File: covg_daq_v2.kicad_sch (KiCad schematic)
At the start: 29 parts

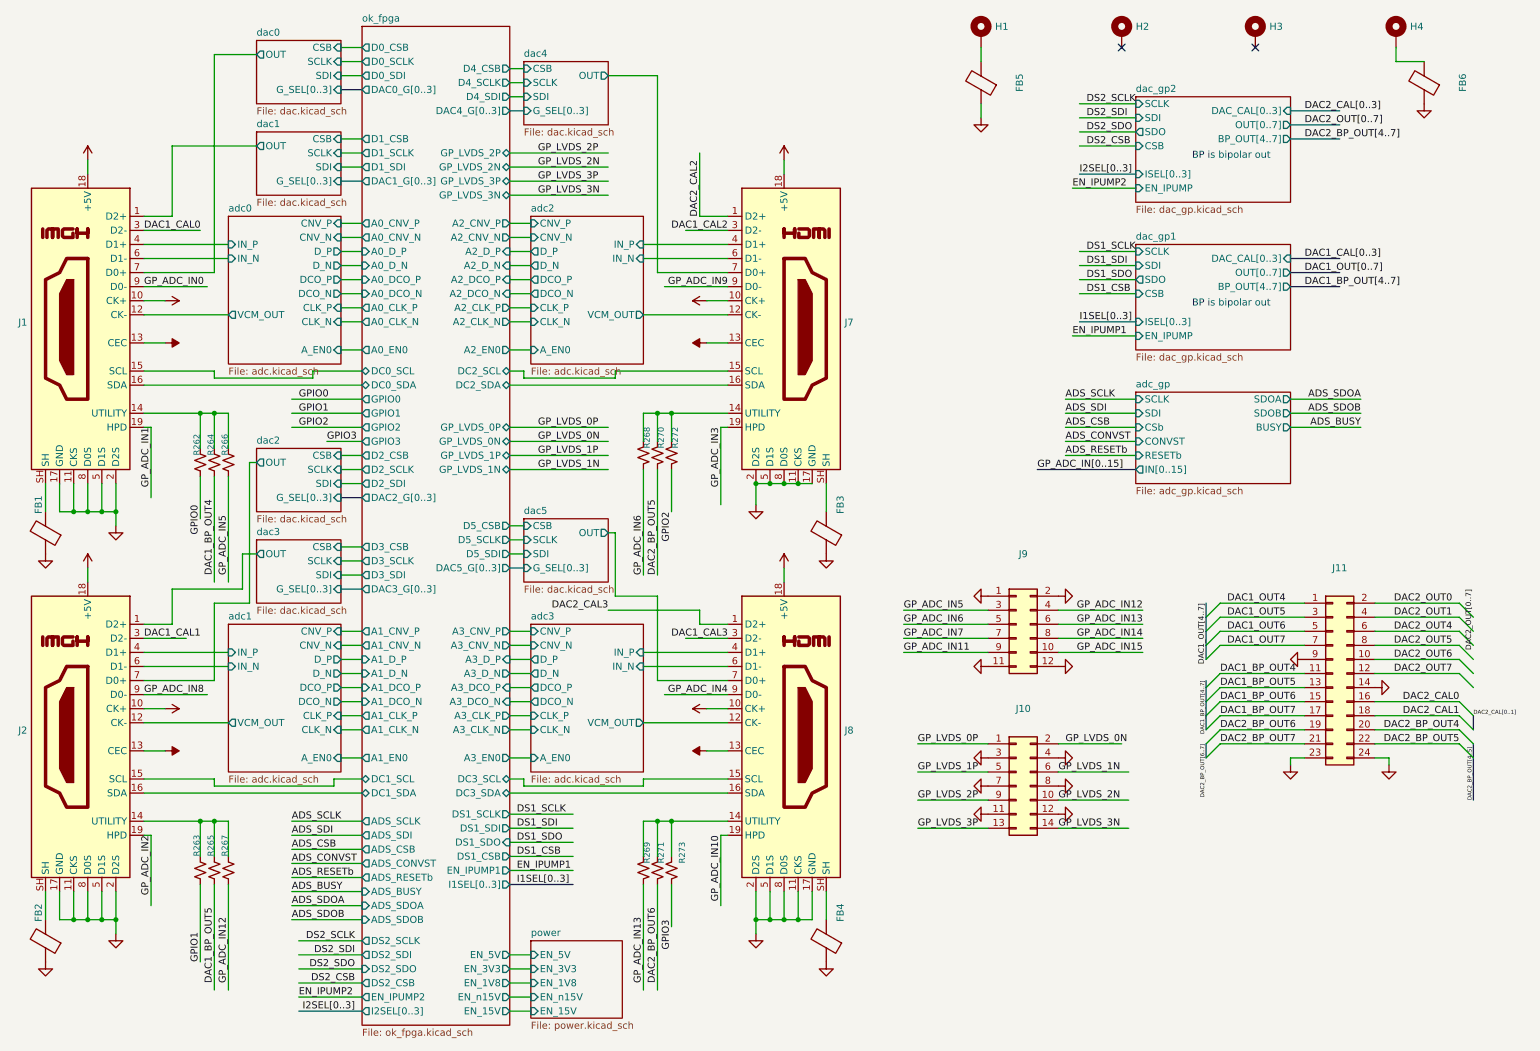
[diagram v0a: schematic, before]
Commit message: closes #31 - incorrect text on Howland current pump. Also, updated fast DAC symbol but not closing until layout is corrected
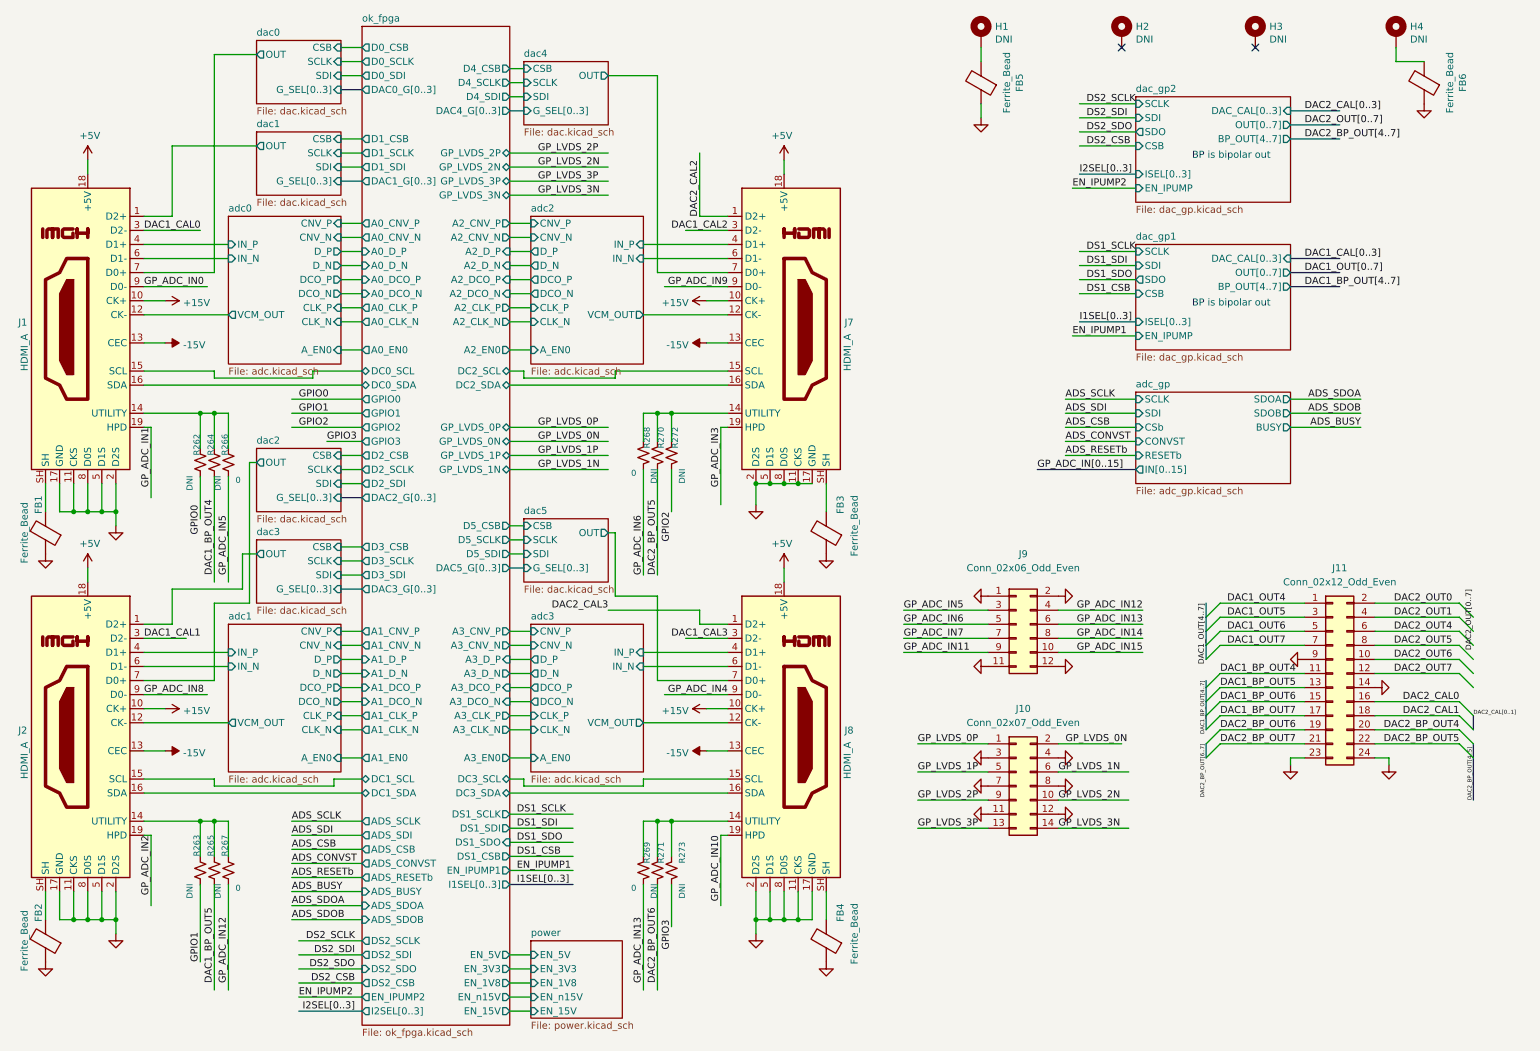
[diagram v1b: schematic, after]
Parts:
- FB1, FB2, FB3, FB4, FB5, FB6: value (none) -> Ferrite_Bead; footprint (none) -> Capacitor_SMD:C_1206_3216Metric
- H1, H2, H3, H4: value (none) -> DNI; footprint (none) -> MountingHole:MountingHole_3.2mm_M3_DIN965_Pad
- J1, J2, J7, J8: value (none) -> HDMI_A; footprint (none) -> covg-kicad:CONN_10029449-111RLF_HDMI_A
- J10: value (none) -> Conn_02x07_Odd_Even; footprint (none) -> Connector_PinHeader_2.00mm:PinHeader_2x07_P2.00mm_Horizontal
- J11: value (none) -> Conn_02x12_Odd_Even; footprint (none) -> Connector_PinHeader_2.00mm:PinHeader_2x12_P2.00mm_Horizontal
- J9: value (none) -> Conn_02x06_Odd_Even; footprint (none) -> Connector_PinHeader_2.00mm:PinHeader_2x06_P2.00mm_Horizontal
- R262, R263, R264, R265, R270, R271, R272, R273: value (none) -> DNI; footprint (none) -> Resistor_SMD:R_0603_1608Metric
- R266, R267, R268, R269: value (none) -> 0; footprint (none) -> Resistor_SMD:R_0603_1608Metric

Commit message: Closes #37 and Closes #25
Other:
- note added: "CH0"
- note added: "CH1"
- note added: "CH2"
- note added: "CH3"
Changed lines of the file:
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@@
     (stroke (width 0) (type default) (color 0 0 0 0))
   )
+  (text "CH2" (at 156.21 43.18 0)
+    (effects (font (size 2.2 2.2)) (justify left bottom))
+  )
   (text "BP is bipolar out" (at 226.06 39.37 0)
     (effects (font (size 1.27 1.27)) (justify left bottom))
   )
+  (text "CH3" (at 156.21 116.84 0)
+    (effects (font (size 2.2 2.2)) (justify left bottom))
+  )
+  (text "CH1" (at 16.51 116.84 0)
+    (effects (font (size 2.2 2.2)) (justify left bottom))
+  )
   (text "BP is bipolar out" (at 226.06 66.04 0)
     (effects (font (size 1.27 1.27)) (justify left bottom))
   )
+  (text "CH0" (at 16.51 43.18 0)
+    (effects (font (size 2.2 2.2)) (justify left bottom))
+  )
   (label "GP_ADC_IN10" (at 140.97 161.29 270)
     (effects (font (size 1.27 1.27)) (justify right bottom))
@@
     )
     (path "/00000000-0000-0000-0000-00006095be10/00000000-0000-0000-0000-0000610c330f"
-      (reference "C20") (unit 1) (value "1u") (footprint "Capacitor_SMD:C_0603_1608Metric")
+      (reference "C20") (unit 1) (value "DNI") (footprint "Capacitor_SMD:C_0603_1608Metric")
     )
     (path "/00000000-0000-0000-0000-00006095be10/00000000-0000-0000-0000-000060de60e5"
@@
     )
     (path "/00000000-0000-0000-0000-00006095be10/00000000-0000-0000-0000-000060f31baa"
-      (reference "D1") (unit 1) (value "D_Schottky") (footprint "Diode_SMD:D_Powermite_AK")
+      (reference "D1") (unit 1) (value "DNI") (footprint "Diode_SMD:D_Powermite_AK")
     )
     (path "/00000000-0000-0000-0000-00006095be10/00000000-0000-0000-0000-0000610e9beb"
-      (reference "D2") (unit 1) (value "D_Schottky") (footprint "Diode_SMD:D_Powermite_AK")
+      (reference "D2") (unit 1) (value "DNI") (footprint "Diode_SMD:D_Powermite_AK")
     )
     (path "/00000000-0000-0000-0000-00006273eef4"
@@
     )
     (path "/00000000-0000-0000-0000-00006095be10/00000000-0000-0000-0000-000060f30942"
-      (reference "L1") (unit 1) (value "4.7u") (footprint "covg-kicad:SRR4018-4R7Y")
+      (reference "L1") (unit 1) (value "DNI") (footprint "covg-kicad:SRR4018-4R7Y")
     )
     (path "/00000000-0000-0000-0000-00006095be10/00000000-0000-0000-0000-000060f31655"
-      (reference "L2") (unit 1) (value "10uH") (footprint "covg-kicad:NRS5020T100MMGJ")
+      (reference "L2") (unit 1) (value "DNI") (footprint "covg-kicad:NRS5020T100MMGJ")
     )
     (path "/00000000-0000-0000-0000-00006095be10/00000000-0000-0000-0000-00006113790e"
-      (reference "L3") (unit 1) (value "15uH") (footprint "covg-kicad:SRR6028-150Y")
+      (reference "L3") (unit 1) (value "DNI") (footprint "covg-kicad:SRR6028-150Y")
     )
     (path "/00000000-0000-0000-0000-00006095a302/00000000-0000-0000-0000-0000da224995"
@@
     )
     (path "/00000000-0000-0000-0000-00006095be10/00000000-0000-0000-0000-000060f42f99"
-      (reference "R35") (unit 1) (value "232k") (footprint "Resistor_SMD:R_0603_1608Metric")
+      (reference "R35") (unit 1) (value "DNI") (footprint "Resistor_SMD:R_0603_1608Metric")
     )
     (path "/00000000-0000-0000-0000-00006095be10/00000000-0000-0000-0000-000060f53569"
@@
     )
     (path "/00000000-0000-0000-0000-00006095be10/00000000-0000-0000-0000-000060bc667f"
-      (reference "R42") (unit 1) (value "249k") (footprint "Resistor_SMD:R_0603_1608Metric")
+      (reference "R42") (unit 1) (value "DNI") (footprint "Resistor_SMD:R_0603_1608Metric")
     )
     (path "/00000000-0000-0000-0000-00006095be10/00000000-0000-0000-0000-000060bb5c7d"
@@
     )
     (path "/00000000-0000-0000-0000-00006095be10/00000000-0000-0000-0000-000060edb97a"
-      (reference "U13") (unit 1) (value "LT3471") (footprint "covg-kicad:DFN-10-1EP_3x3mm_P0.5mm_EP1.65x2.38mm")
+      (reference "U13") (unit 1) (value "DNI") (footprint "covg-kicad:DFN-10-1EP_3x3mm_P0.5mm_EP1.65x2.38mm")
     )
     (path "/00000000-0000-0000-0000-00006095be10/00000000-0000-0000-0000-0000614d3f9b"
